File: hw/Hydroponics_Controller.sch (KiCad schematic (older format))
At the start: 31 parts, among them K1 1Wire, K2 1Wire, P1 I2C, P2 I2C, P3 Relay, P4 LowWater, P5 Tank1High, P6 Tank2High, P7 eTape, P8 Power_In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

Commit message: Added RTC to board. Corrected error using A6/A7 as digital pins...
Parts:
- added BT1: BATTERY, symbol BATTERY
- added C6: 0.1uF, symbol C
- added R10, R9: 10k, symbol R
- added U3: DS3231, symbol DS3231
- R3, R4: value 4k7 -> 10k
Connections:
- wire segments 127 -> 142
- no-connect marks 4 -> 5
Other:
- note added: "Real time clock"
- moved on the sheet: P8

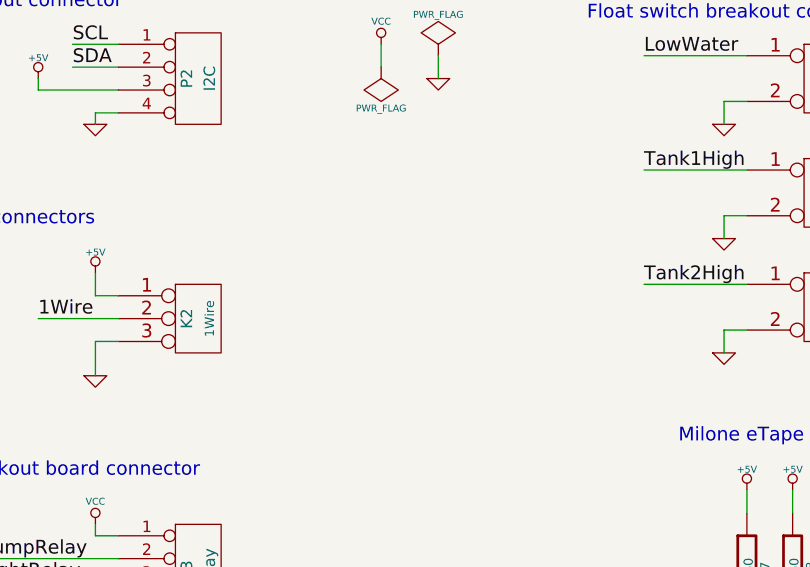
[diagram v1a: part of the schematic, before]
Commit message: Fixed the missing pullup resistor from the 1 wire connector
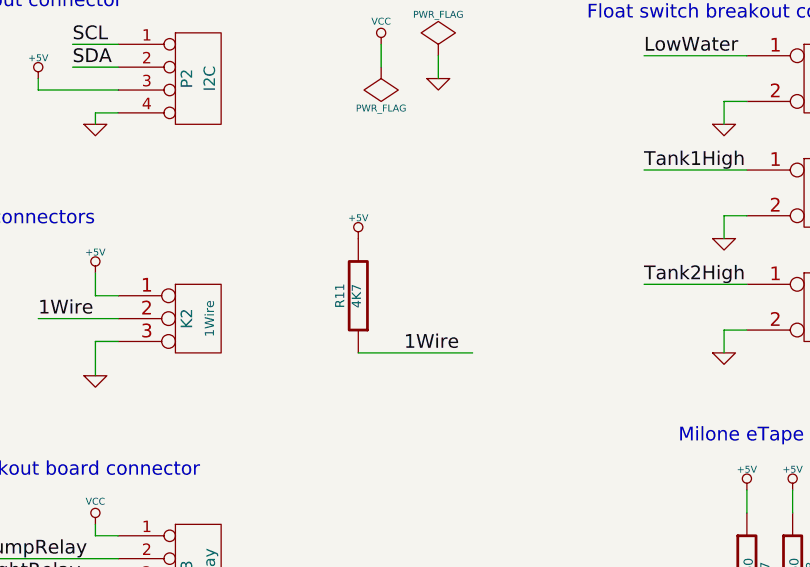
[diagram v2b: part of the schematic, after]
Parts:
- added R11: 4K7, symbol R
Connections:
- wire segments 142 -> 143
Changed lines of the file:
@@
 Wire Wire Line
 	5650 4350 5650 4300
+$Comp
+L R R11
+U 1 1 53DE9952
+P 8300 2250
+F 0 "R11" V 8380 2250 40  0000 C CNN
+F 1 "4K7" V 8307 2251 40  0000 C CNN
+F 2 "" V 8230 2250 30  0000 C CNN
+F 3 "" H 8300 2250 30  0000 C CNN
+	1    8300 2250
+	-1   0    0    1
+$EndComp
+Wire Wire Line
+	8300 2500 8800 2500
+Text Label 8500 2500 0    60   ~ 0
+1Wire
+$Comp
+L +5V #PWR054
+U 1 1 53DE9A06
+P 8300 2000
+F 0 "#PWR054" H 8300 2090 20  0001 C CNN
+F 1 "+5V" H 8300 2090 30  0000 C CNN
+F 2 "" H 8300 2000 60  0000 C CNN
+F 3 "" H 8300 2000 60  0000 C CNN
+	1    8300 2000
+	1    0    0    -1
+$EndComp
 $EndSCHEMATC

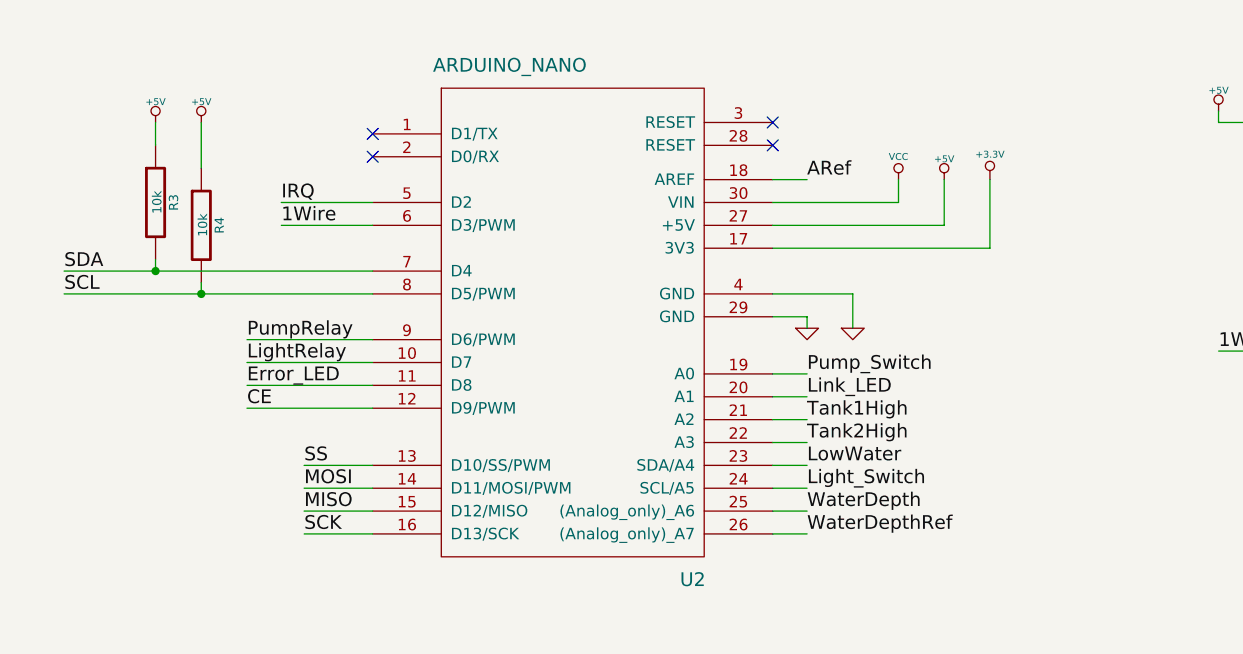
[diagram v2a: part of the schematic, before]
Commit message: updated to fix I2C connected to wrong pins. Also changed cap to 0402
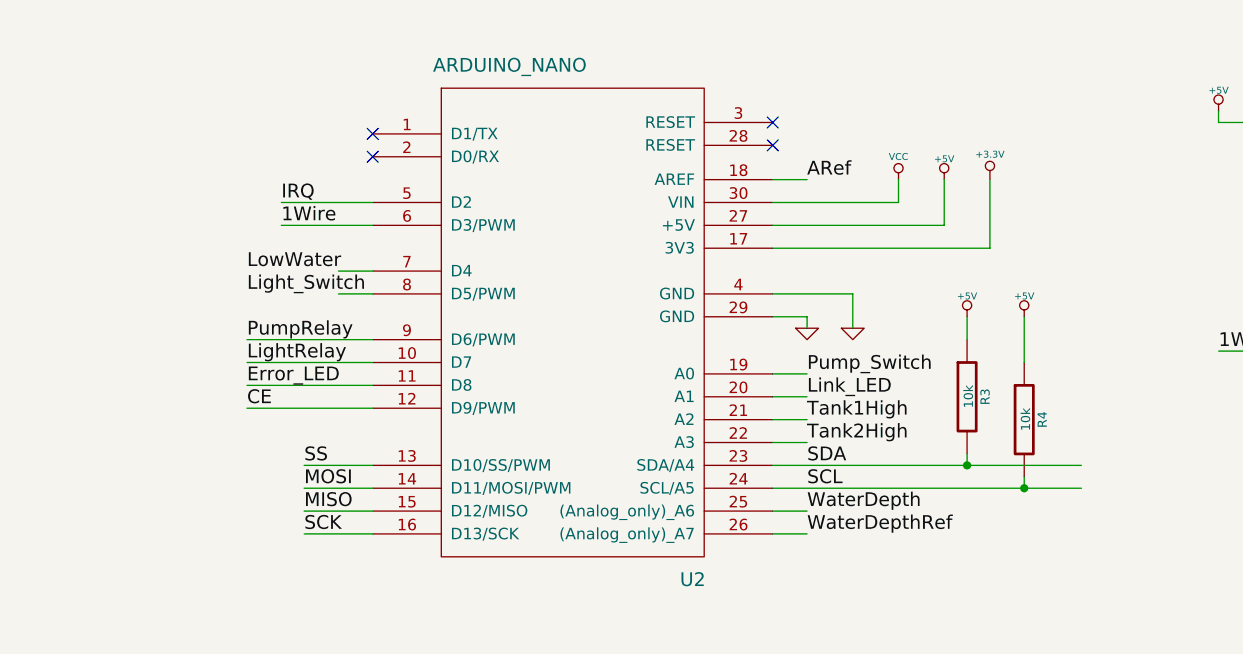
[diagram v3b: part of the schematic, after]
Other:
- moved on the sheet: R3, R4
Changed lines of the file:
@@
 L R R4
 U 1 1 53B8229E
-P 1450 1800
-F 0 "R4" V 1530 1800 40  0000 C CNN
-F 1 "10k" V 1457 1801 40  0000 C CNN
-F 2 "" V 1380 1800 30  0000 C CNN
-F 3 "" H 1450 1800 30  0000 C CNN
-	1    1450 1800
+P 5050 2650
+F 0 "R4" V 5130 2650 40  0000 C CNN
+F 1 "10k" V 5057 2651 40  0000 C CNN
+F 2 "" V 4980 2650 30  0000 C CNN
+F 3 "" H 5050 2650 30  0000 C CNN
+	1    5050 2650
 	1    0    0    -1
 $EndComp
@@
 L R R3
 U 1 1 53B822B2
-P 1250 1700
-F 0 "R3" V 1330 1700 40  0000 C CNN
-F 1 "10k" V 1257 1701 40  0000 C CNN
-F 2 "" V 1180 1700 30  0000 C CNN
-F 3 "" H 1250 1700 30  0000 C CNN
-	1    1250 1700
+P 4800 2550
+F 0 "R3" V 4880 2550 40  0000 C CNN
+F 1 "10k" V 4807 2551 40  0000 C CNN
+F 2 "" V 4730 2550 30  0000 C CNN
+F 3 "" H 4800 2550 30  0000 C CNN
+	1    4800 2550
 	1    0    0    -1
 $EndComp
@@
 Text Label 1800 1800 0    60   ~ 0
 1Wire
-Text Label 850  2000 0    60   ~ 0
+Text Label 4100 2850 0    60   ~ 0
 SDA
-Text Label 850  2100 0    60   ~ 0
+Text Label 4100 2950 0    60   ~ 0
 SCL
 Text Label 1650 2300 0    60   ~ 0
@@
 Text Label 4100 2750 0    60   ~ 0
 Tank2High
-Text Label 4100 2850 0    60   ~ 0
+Text Label 1650 2000 0    60   ~ 0
 LowWater
-Text Label 4100 2950 0    60   ~ 0
+Text Label 1650 2100 0    60   ~ 0
 Light_Switch
 Text Label 4100 2450 0    60   ~ 0
@@
 	2200 1800 1800 1800
 Wire Wire Line
-	2200 2000 850  2000
-Wire Wire Line
-	1250 2000 1250 1950
-Connection ~ 1250 2000
-Wire Wire Line
-	2200 2100 850  2100
-Wire Wire Line
-	1450 2100 1450 2050
-Connection ~ 1450 2100
+	5300 2850 3950 2850
+Wire Wire Line
+	4800 2850 4800 2800
+Connection ~ 4800 2850
+Wire Wire Line
+	5300 2950 3950 2950
+Wire Wire Line
+	5050 2950 5050 2900
+Connection ~ 5050 2950
 Wire Wire Line
 	2200 2300 1650 2300
@@
 	3950 2450 4100 2450
 Wire Wire Line
-	3950 2950 4100 2950
-Wire Wire Line
-	3950 2850 4100 2850
+	2050 2100 2200 2100
+Wire Wire Line
+	2050 2000 2200 2000
 Wire Wire Line
 	3950 2750 4100 2750
@@
 L +5V #PWR039
 U 1 1 53B82F25
-P 1250 1350
-F 0 "#PWR039" H 1250 1440 20  0001 C CNN
-F 1 "+5V" H 1250 1440 30  0000 C CNN
-F 2 "" H 1250 1350 60  0000 C CNN
-F 3 "" H 1250 1350 60  0000 C CNN
-	1    1250 1350
+P 4800 2200
+F 0 "#PWR039" H 4800 2290 20  0001 C CNN
+F 1 "+5V" H 4800 2290 30  0000 C CNN
+F 2 "" H 4800 2200 60  0000 C CNN
+F 3 "" H 4800 2200 60  0000 C CNN
+	1    4800 2200
 	1    0    0    -1
 $EndComp
@@
 L +5V #PWR040
 U 1 1 53B82F39
-P 1450 1350
-F 0 "#PWR040" H 1450 1440 20  0001 C CNN
-F 1 "+5V" H 1450 1440 30  0000 C CNN
-F 2 "" H 1450 1350 60  0000 C CNN
-F 3 "" H 1450 1350 60  0000 C CNN
-	1    1450 1350
-	1    0    0    -1
-$EndComp
-Wire Wire Line
-	1450 1550 1450 1350
-Wire Wire Line
-	1250 1450 1250 1350
+P 5050 2200
+F 0 "#PWR040" H 5050 2290 20  0001 C CNN
+F 1 "+5V" H 5050 2290 30  0000 C CNN
+F 2 "" H 5050 2200 60  0000 C CNN
+F 3 "" H 5050 2200 60  0000 C CNN
+	1    5050 2200
+	1    0    0    -1
+$EndComp
+Wire Wire Line
+	5050 2400 5050 2200
+Wire Wire Line
+	4800 2300 4800 2200
 $Comp
 L GND #PWR041
